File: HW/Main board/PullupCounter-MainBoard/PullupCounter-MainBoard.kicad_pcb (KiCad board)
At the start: 2 copper layers, 54 parts, among them J1 Barrel_Jack_Switch, J2 FTDI-Cable-Header, J3 8P8C, SW1 SW_Push, U1 ATMEGA328P-AU-Arduino, U2 DS1307Z+, U3 AMS117-5.0, U4 74HC14, U5 8x8-LEDArray, U6 DS92LV010A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

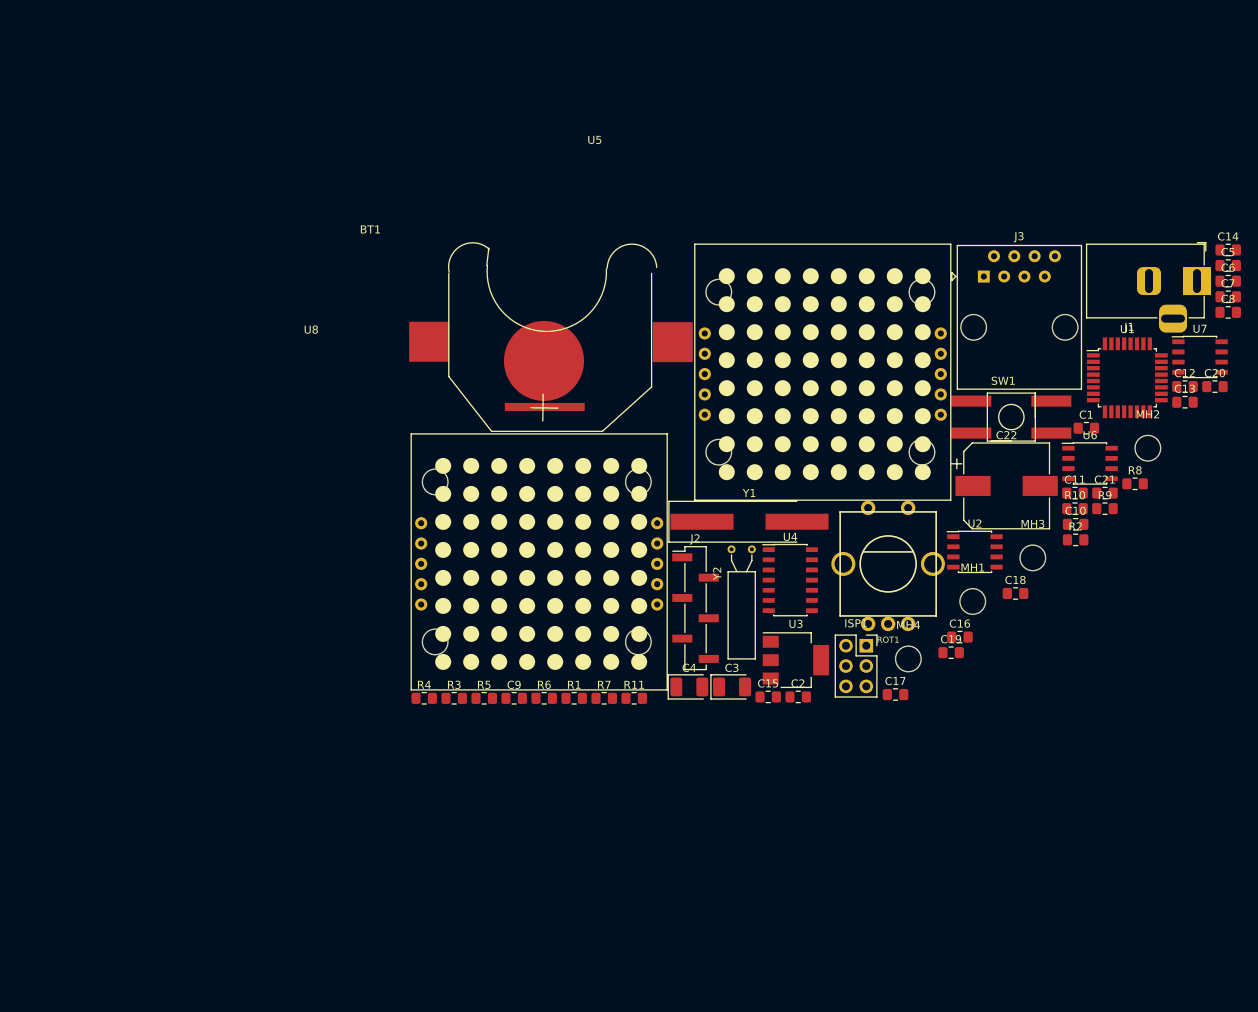
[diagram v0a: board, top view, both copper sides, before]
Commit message: Layout started
Need to committo a board size and hole pattern
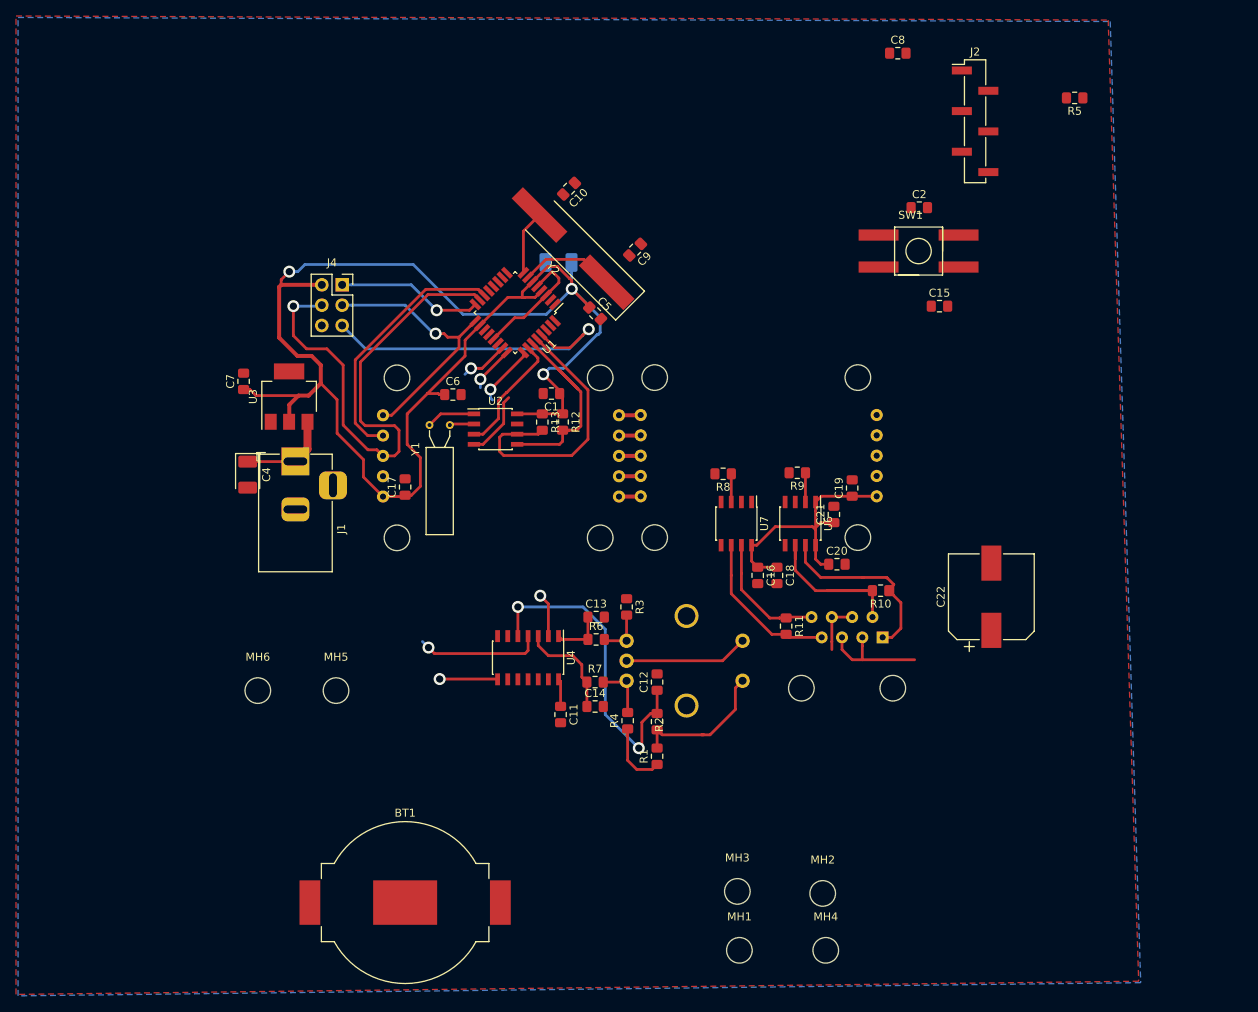
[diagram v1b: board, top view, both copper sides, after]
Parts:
- removed ISP1: ISP-header, Connector_PinSocket_2.54mm:PinSocket_2x03_P2.54mm_Vertical
- added J4: AVR-ISP-6, Connector_PinSocket_2.54mm:PinSocket_2x03_P2.54mm_Vertical, F.Cu at (108.1, 70.6)
- added MH5: StripsFäste, MountingHole:MountingHole_3.2mm_M3, F.Cu at (107.3, 121.3)
- added MH6: StripsFäste, MountingHole:MountingHole_3.2mm_M3, F.Cu at (97.5, 121.3)
- added R12: 4k7, Resistor_SMD:R_0805_2012Metric_Pad1.15x1.40mm_HandSolder, F.Cu at (135.6, 87.8)
- added R13: 4k7, Resistor_SMD:R_0805_2012Metric_Pad1.15x1.40mm_HandSolder, F.Cu at (133.1, 87.8)
- BT1: footprint Libs:Cheap_CR2032_holder -> Battery:BatteryHolder_MPD_BC2003_1x2032
- C3, J3, ROT1, U5, U8: moved to B.Cu
- Y1: footprint Crystal:Crystal_SMD_HC49-SD_HandSoldering -> Crystal:Crystal_AT310_D3.0mm_L10.0mm_Horizontal
- Y2: footprint Crystal:Crystal_AT310_D3.0mm_L10.0mm_Horizontal -> Crystal:Crystal_SMD_HC49-SD_HandSoldering
- moved C7 123.5 mm to (95.8, 82.7), turned to 90 degrees
- moved J1 114.9 mm to (102.2, 92.7), turned to 90 degrees
- moved R5 105.3 mm to (199.6, 47.2), turned to 180 degrees
- moved C6 97.9 mm to (121.9, 84.3)
- moved C14 97.6 mm to (139.7, 123.3)
- moved C5 79.4 mm to (139.7, 74.2), turned to 315 degrees
- moved C13 78.4 mm to (139.8, 112.1)
- moved U1 77.0 mm to (129.7, 74.1), turned to 225 degrees
- moved C10 76.0 mm to (136.4, 58.6), turned to 225 degrees
- moved C12 75.6 mm to (147.4, 120.3), turned to 90 degrees
- moved U3 71.4 mm to (101.4, 84.6), turned to 90 degrees
- moved J2 70.2 mm to (187.2, 50.2)
- moved BT1 70.2 mm to (116.0, 147.8)
- moved C11 70.0 mm to (135.4, 124.3), turned to 270 degrees
- moved MH2 68.9 mm to (168.1, 146.7)
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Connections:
- J3 pad 7: Echo+ -> Echo-
- J3 pad 8: Echo- -> Echo+
- U4 pad 14: (no net) -> VCC
- U4 pad 7: (no net) -> GND
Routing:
- net VCC: track 0.00 -> 227.3 mm, vias 0 -> 3
- net MOSI: track 0.00 -> 65.4 mm, vias 0 -> 1
- net GND: track 0.00 -> 45.9 mm
- net Net-(C12-Pad1): track 0.00 -> 41.0 mm, vias 0 -> 2
- net reset_in: track 0.00 -> 40.6 mm, vias 0 -> 1
- net scl: track 0.00 -> 34.8 mm
- net SCK: track 0.00 -> 33.5 mm, vias 0 -> 1
- net CS: track 0.00 -> 32.1 mm
- net sda: track 0.00 -> 26.1 mm
- net +12V: track 0.00 -> 25.5 mm
- net Trig-: track 0.00 -> 24.5 mm
- net Trig+: track 0.00 -> 24.0 mm
- net encB: track 0.00 -> 21.6 mm, vias 0 -> 2
- net Echo-: track 0.00 -> 19.6 mm
- net MISO: track 0.00 -> 18.3 mm, vias 0 -> 1
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- added copper zone on B.Cu, net GND
- added copper zone on F.Cu, net GND
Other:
- net class Default: clearance 0.2 -> 0.3; trace_width 0.25 -> 0.35; via_dia 0.8 -> 1.5; via_drill 0.4 -> 0.91
- net class VIN added: clearance 0.4, trace_width 0.8, via_dia 2, via_drill 0.91
- rule trace_clearance: 0.2 -> 0.3

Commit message: Mainboard
Version 1 of mainboard done
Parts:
- J1: moved to B.Cu
- moved MH1 113.0 mm to (96.6, 58.7)
- moved MH4 96.8 mm to (186.3, 58.7)
- moved BT1 90.1 mm to (186.6, 91.8), turned to 90 degrees
- moved C8 76.1 mm to (105.7, 66.8)
- moved MH3 63.2 mm to (96.6, 129.4)
- moved C2 61.7 mm to (121.5, 80.0), turned to 270 degrees
- moved J2 41.5 mm to (159.9, 81.4), turned to 90 degrees
- moved R5 39.0 mm to (172.6, 75.3), turned to 90 degrees
- moved MH2 25.2 mm to (186.6, 129.4)
- moved SW1 21.6 mm to (154.3, 70.1)
- moved C15 13.1 mm to (169.8, 75.3), turned to 90 degrees
- moved C7 9.33 mm to (100.3, 90.8), turned to 180 degrees
- moved C17 6.52 mm to (110.5, 99.4), turned to 270 degrees
- moved C14 5.72 mm to (139.8, 117.6)
- moved C22 5.57 mm to (186.1, 114.2)
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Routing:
- net VCC: track 227.3 -> 400.6 mm, vias 3 -> 4
- net +BATT: track 15.3 -> 130.1 mm, vias 0 -> 2
- net +12V: track 25.5 -> 130.1 mm, vias 0 -> 1
- net Echo: track 3.53 -> 89.4 mm, vias 0 -> 2
- net Trig: track 3.65 -> 81.0 mm, vias 0 -> 2
- net reset_in: track 40.6 -> 82.4 mm
- net TX0: track 0.00 -> 38.4 mm, vias 0 -> 2
- net encBTN: track 13.3 -> 49.8 mm
- net RXI: track 0.00 -> 30.5 mm, vias 0 -> 2
- net encA: track 13.2 -> 40.5 mm
- net GND: track 45.9 -> 71.2 mm, vias 0 -> 1
- net encB: track 21.6 -> 39.3 mm
- net Trig-: track 24.5 -> 18.4 mm
- net Net-(C2-Pad1): track 0.00 -> 5.79 mm
- net RST: track 0.00 -> 5.41 mm
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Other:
- board outline added: 97 x 77.9 mm
- board text added: "Pullup counter 24/8-18"
